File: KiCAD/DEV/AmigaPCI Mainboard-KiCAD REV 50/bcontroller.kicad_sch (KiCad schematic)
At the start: 32 parts, among them CN409 SPI, J901 IDE MODES, U111 74LVC16646, U112 74LVC16646, U409 ICE40HX4K-TQ144, U409F1 W25X20CLSN

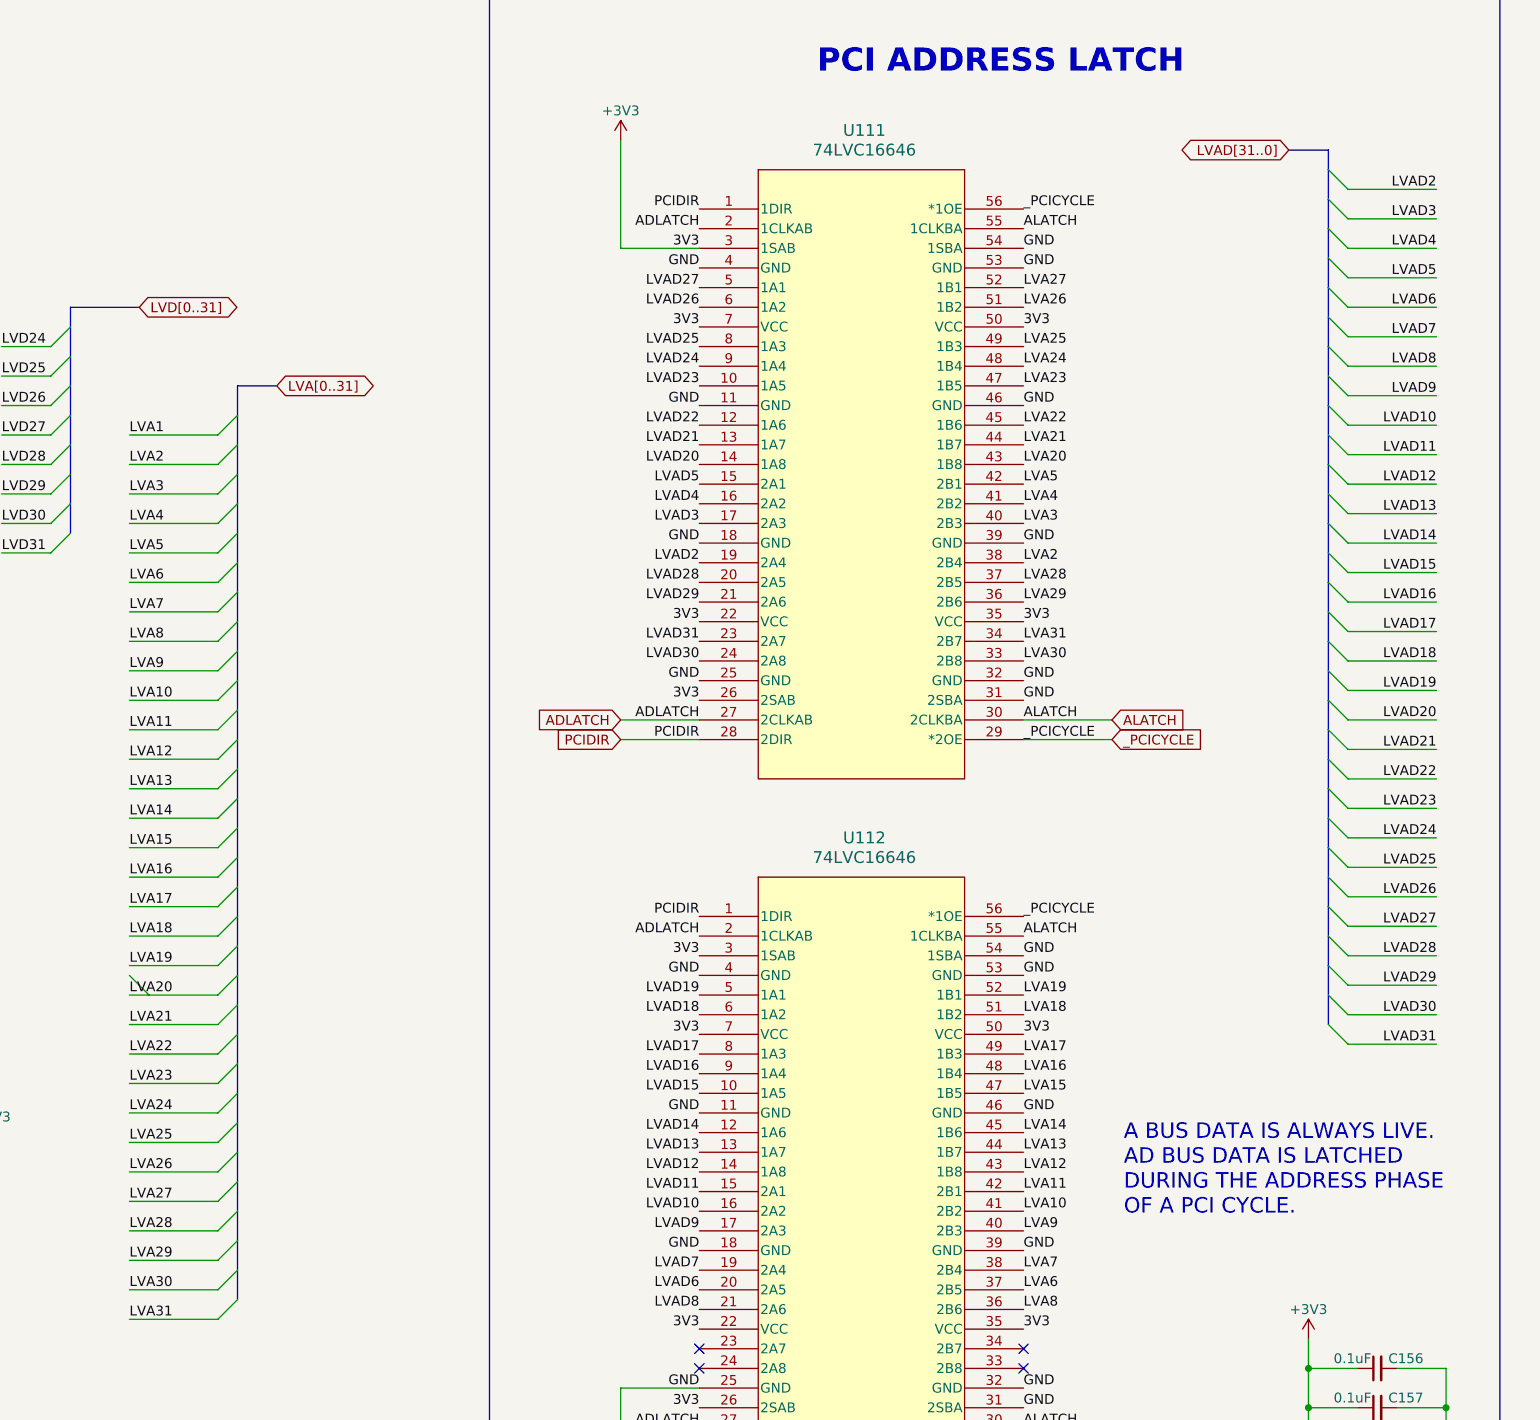
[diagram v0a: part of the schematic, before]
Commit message: Updated STM32F205 microcontroller.
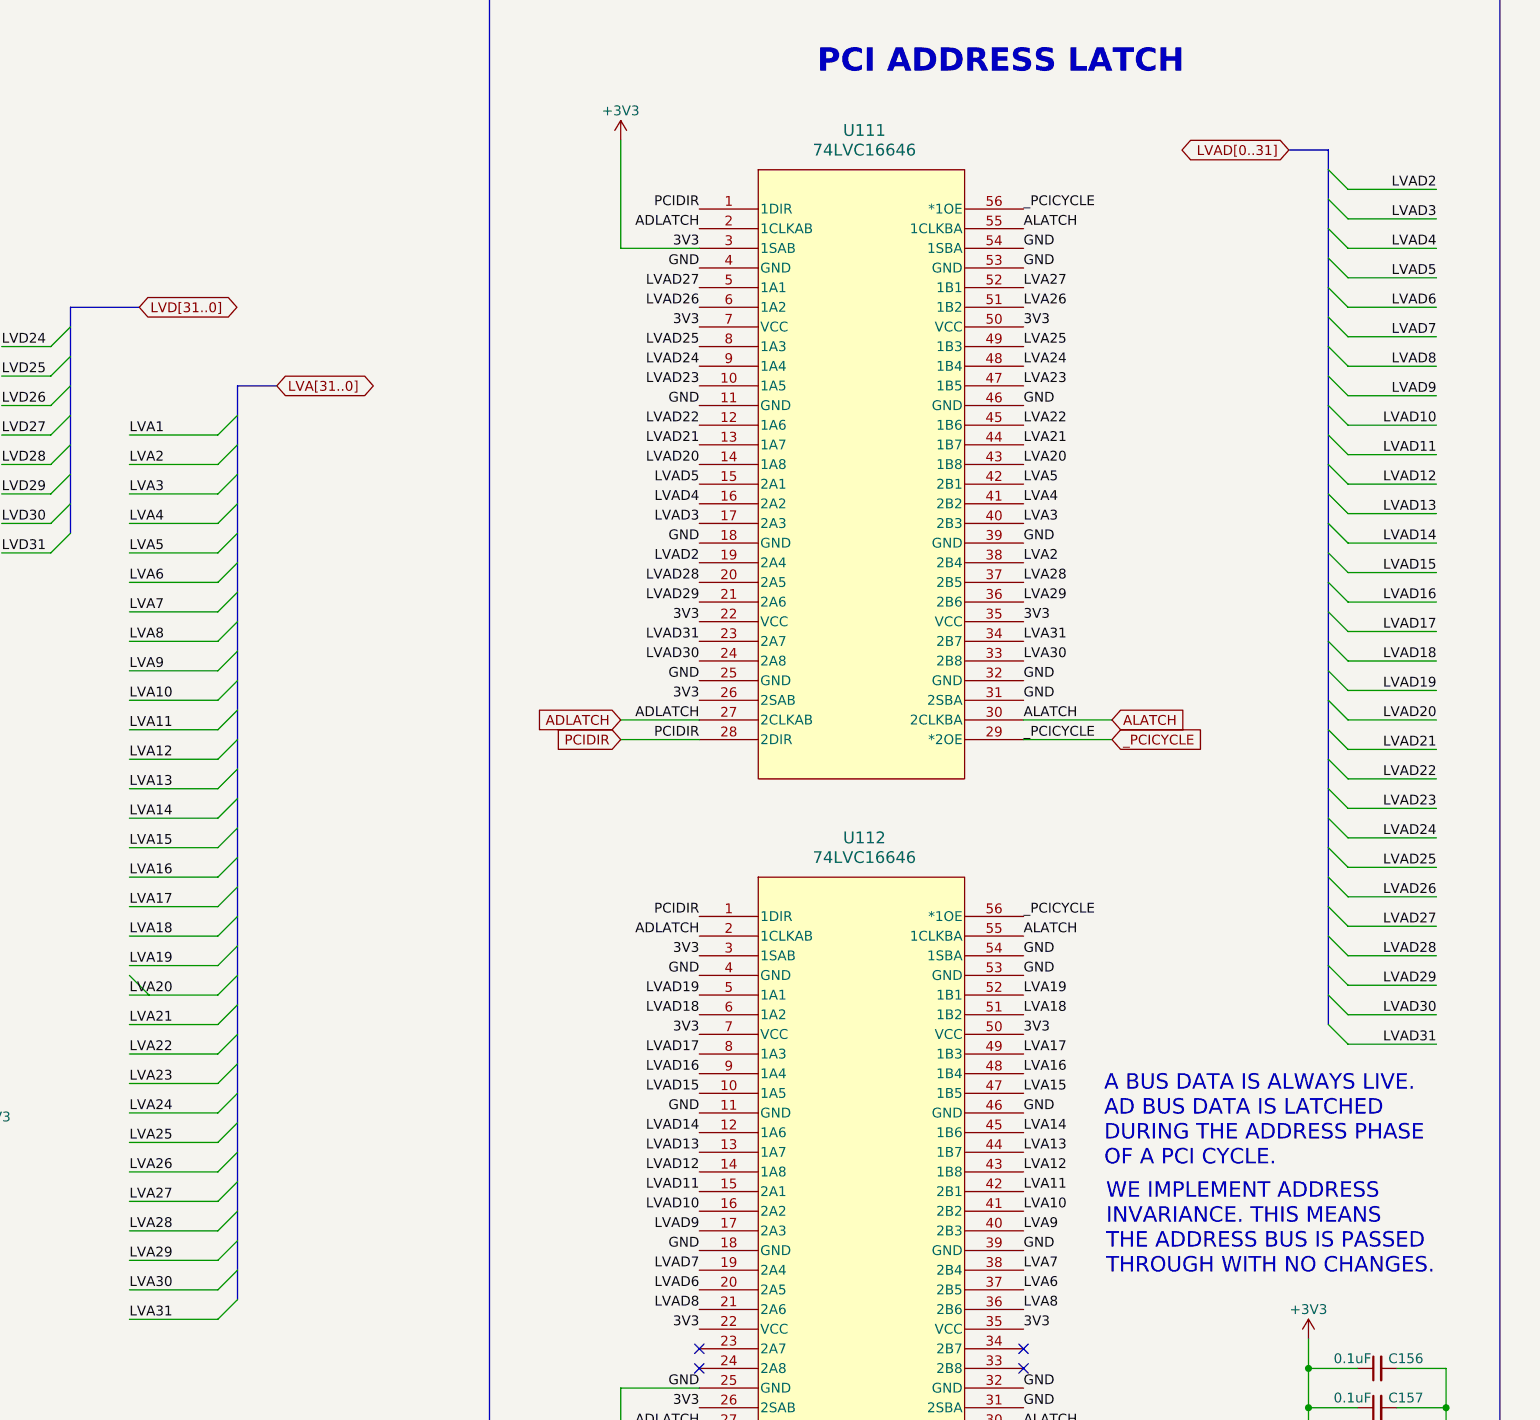
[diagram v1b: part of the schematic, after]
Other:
- note added: "WE IMPLEMENT ADDRESS INVARIANCE. THIS MEANS THE ADDRESS BUS IS PASSED THROUGH WITH NO CHANGES."
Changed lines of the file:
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@@
 	(text "A BUS DATA IS ALWAYS LIVE.\nAD BUS DATA IS LATCHED\nDURING THE ADDRESS PHASE \nOF A PCI CYCLE."
 		(exclude_from_sim no)
-		(at 354.584 175.006 0)
+		(at 352.044 168.656 0)
 		(effects
 			(font
@@
 		)
 	)
+	(text "WE IMPLEMENT ADDRESS\nINVARIANCE. THIS MEANS\nTHE ADDRESS BUS IS PASSED \nTHROUGH WITH NO CHANGES."
+		(exclude_from_sim no)
+		(at 352.298 182.626 0)
+		(effects
+			(font
+				(size 2 2)
+			)
+			(justify left)
+		)
+	)
 	(text "J901"
 		(exclude_from_sim no)
@@
 		)
 	)
-	(global_label "LVD[0..31]"
+	(global_label "LVD[31..0]"
 		(shape bidirectional)
 		(at 227.33 63.5 0)
@@
 		)
 	)
-	(global_label "LVAD[31..0]"
+	(global_label "LVAD[0..31]"
 		(shape bidirectional)
 		(at 375.92 43.18 180)
@@
 		)
 	)
-	(global_label "LVA[0..31]"
+	(global_label "LVA[31..0]"
 		(shape bidirectional)
 		(at 245.11 73.66 0)
